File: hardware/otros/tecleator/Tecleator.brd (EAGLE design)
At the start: 96.5 x 56.8 mm, 53 parts, among them T1 BC547

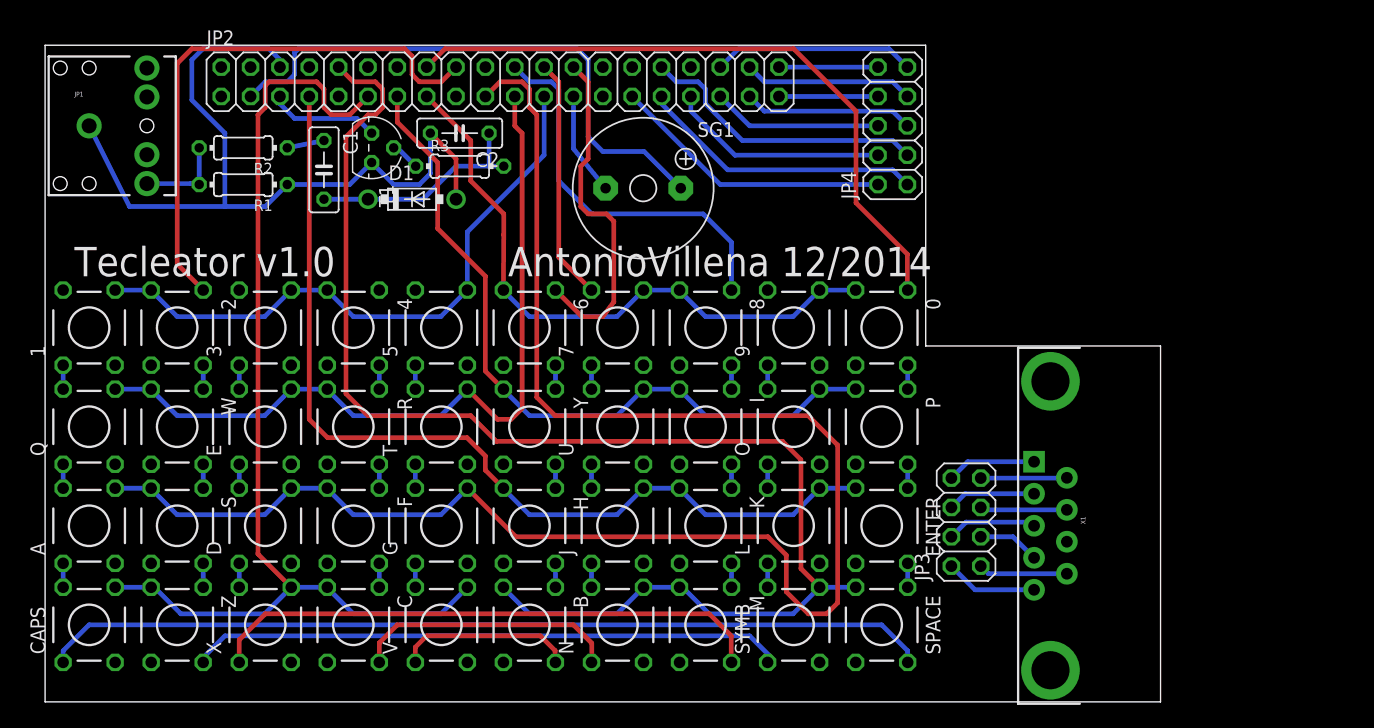
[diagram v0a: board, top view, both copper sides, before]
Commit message: 
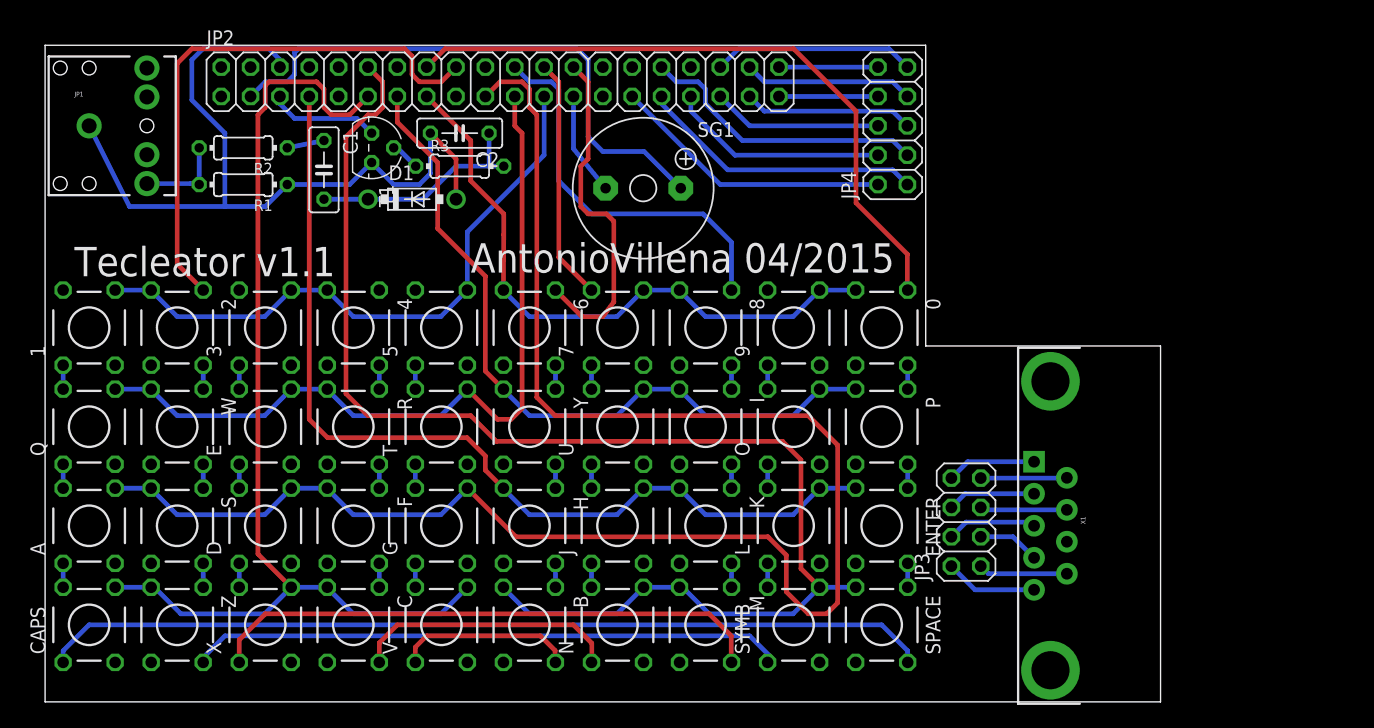
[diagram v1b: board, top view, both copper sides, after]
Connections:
- net VET: now also JP2.12; no longer JP2.10
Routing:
- net VET: track 120.4 -> 118.3 mm
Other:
- board text added: "AntonioVillena 04/2015"
- board text added: "Tecleator v1.1"
- board text removed: "Tecleator v1.0 AntonioVillena 12/2014"
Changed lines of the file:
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@@
 <wire x1="76.18" y1="55.2325" x2="0" y2="55.2325" width="0" layer="20"/>
 <wire x1="0" y1="55.2325" x2="0" y2="-1.5875" width="0" layer="20"/>
-<text x="2.54" y="35.2425" size="2.54" layer="25">Tecleator v1.0               AntonioVillena 12/2014</text>
+<text x="2.54" y="35.2425" size="2.54" layer="25">Tecleator v1.1</text>
 <wire x1="0" y1="-1.5875" x2="96.52" y2="-1.5875" width="0" layer="20"/>
 <wire x1="76.2" y1="55.245" x2="76.2" y2="29.21" width="0" layer="20"/>
 <wire x1="76.2" y1="29.21" x2="96.52" y2="29.21" width="0" layer="20"/>
 <wire x1="96.52" y1="29.21" x2="96.52" y2="-1.5875" width="0" layer="20"/>
+<text x="36.83" y="35.56" size="2.54" layer="25">AntonioVillena 04/2015</text>
 </plain>
 <attributes>
@@
 <wire x1="57.4675" y1="6.0325" x2="64.7225" y2="6.0325" width="0.4064" layer="16"/>
 <wire x1="64.7225" y1="6.0325" x2="67.02" y2="8.33" width="0.4064" layer="16"/>
-<contactref element="JP2" pad="10"/>
-<wire x1="25.4" y1="53.34" x2="26.67" y2="52.07" width="0.4064" layer="1"/>
-<wire x1="26.67" y1="52.07" x2="28.575" y2="52.07" width="0.4064" layer="1"/>
-<wire x1="28.575" y1="52.07" x2="29.21" y2="51.435" width="0.4064" layer="1"/>
-<wire x1="29.21" y1="51.435" x2="29.21" y2="49.8475" width="0.4064" layer="1"/>
+<wire x1="29.21" y1="52.07" x2="29.21" y2="49.8475" width="0.4064" layer="1"/>
 <wire x1="29.21" y1="49.8475" x2="28.575" y2="49.2125" width="0.4064" layer="1"/>
 <wire x1="28.575" y1="49.2125" x2="27.94" y2="49.2125" width="0.4064" layer="1"/>
@@
 <wire x1="65.405" y1="19.3675" x2="65.405" y2="9.945" width="0.4064" layer="1"/>
 <wire x1="65.405" y1="9.945" x2="67.02" y2="8.33" width="0.4064" layer="1"/>
+<contactref element="JP2" pad="12"/>
+<wire x1="29.21" y1="52.07" x2="27.94" y2="53.34" width="0.4064" layer="1"/>
 </signal>
 <signal name="N$1">
